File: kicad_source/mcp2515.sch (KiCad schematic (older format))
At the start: 8 parts, among them U8 MCP2515, U9 SN65HVD232, Y1 16MHz

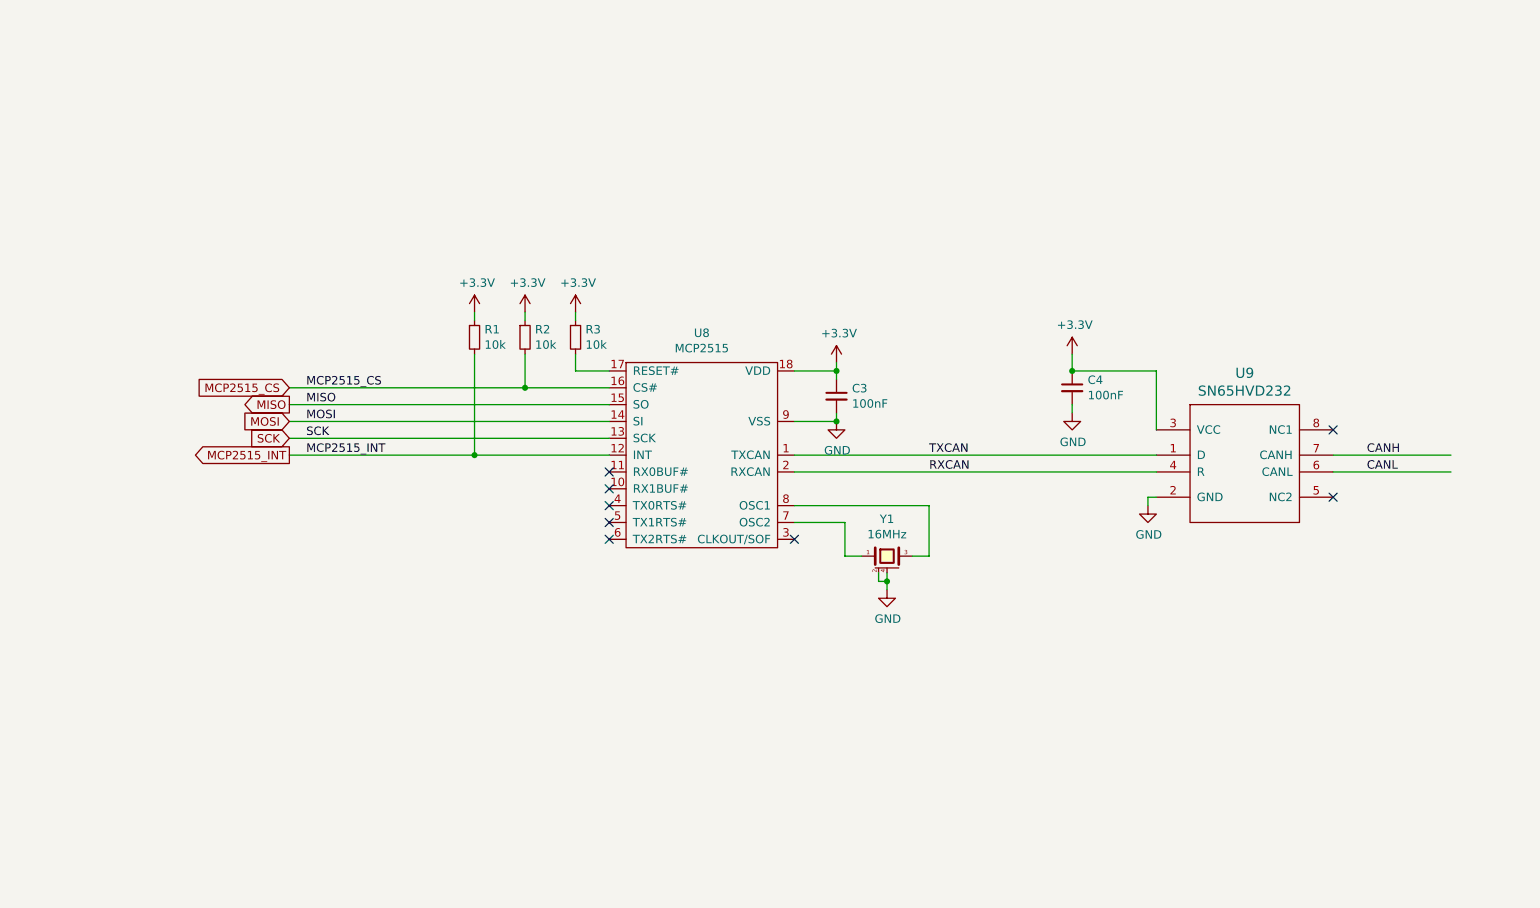
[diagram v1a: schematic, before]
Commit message: added dronecode can and qwiic connectors
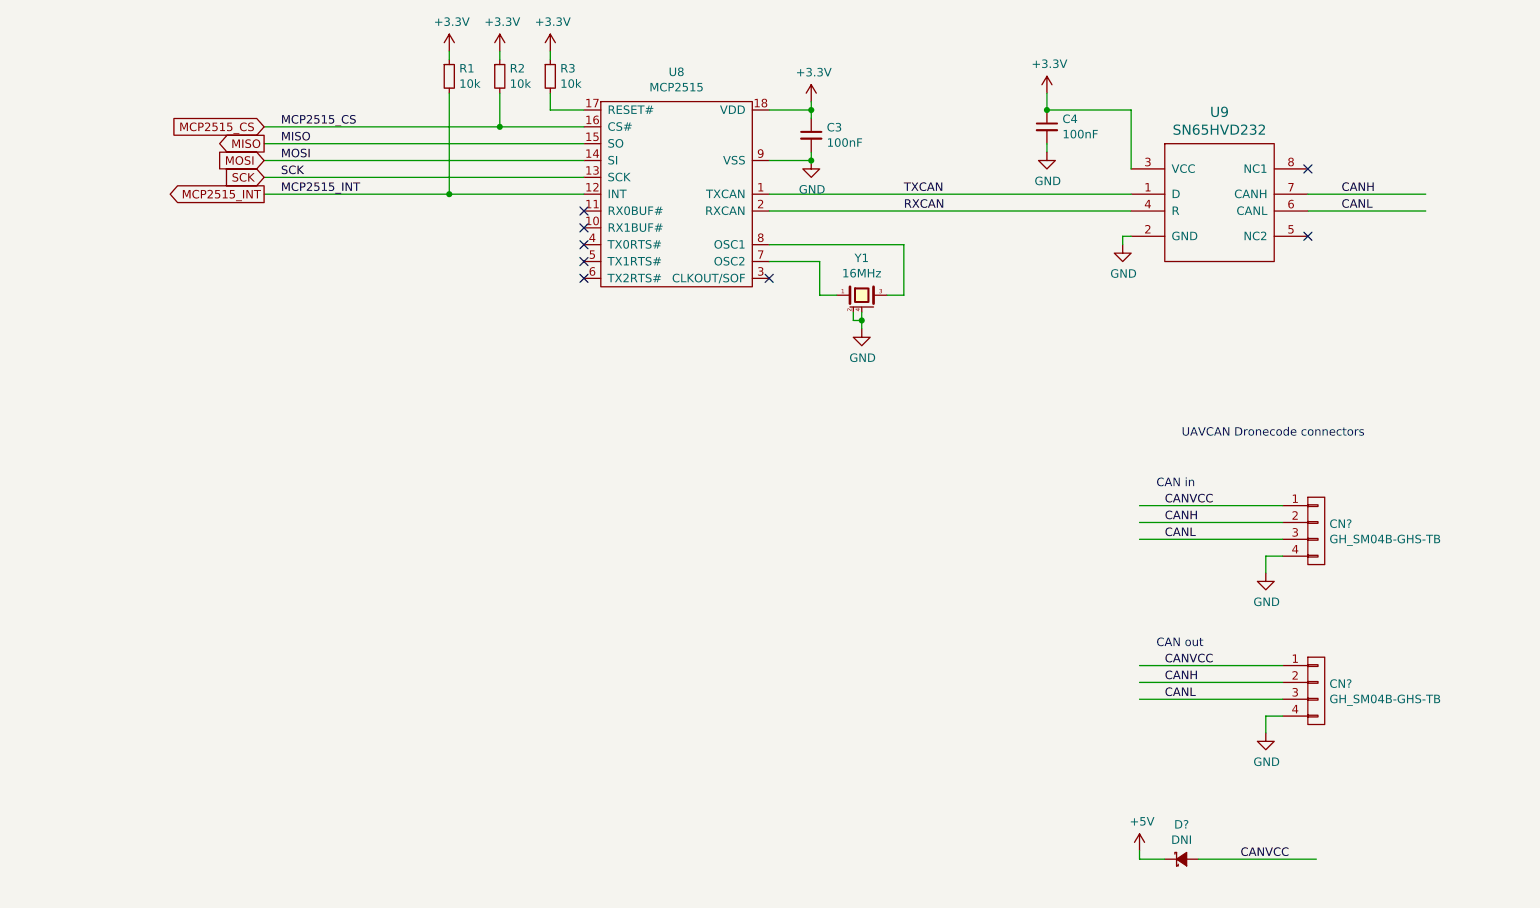
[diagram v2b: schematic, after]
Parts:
- added CN? (x2): GH_SM04B-GHS-TB, Connector_JST:JST_GH_SM04B-GHS-TB_1x04-1MP_P1.25mm_Horizontal, symbol mechanical-connectors:CONN_01X04
- added D?: DNI, diodes:SOD-123, symbol devices:D_Schottky_Small
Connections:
- net labels added: +5V, CANVCC
- wire segments 39 -> 52
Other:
- note added: "CAN in"
- note added: "CAN out"
- note added: "UAVCAN Dronecode connectors"
- moved on the sheet: C3, C4, R1, R2, R3, U8, U9, Y1

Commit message: added eeprom and servo connectors, updated pdf
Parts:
- added C7, C8: 10pF, capacitors:C_0603, symbol devices:C_0603
- gave numbers to parts that had none: 3
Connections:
- wire segments 52 -> 56
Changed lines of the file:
@@
 P 8800 4200
 AR Path="/624F7A5F/62500CA8" Ref="CN?"  Part="1"
-AR Path="/5ED92F9C/62500CA8" Ref="CN?"  Part="1"
-F 0 "CN?" H 8878 4241 50  0000 L CNN
+AR Path="/5ED92F9C/62500CA8" Ref="CN4"  Part="1"
+F 0 "CN4" H 8878 4241 50  0000 L CNN
 F 1 "GH_SM04B-GHS-TB" H 8878 4150 50  0000 L CNN
 F 2 "Connector_JST:JST_GH_SM04B-GHS-TB_1x04-1MP_P1.25mm_Horizontal" H 8800 4200 50  0001 C CNN
@@
 P 8500 4450
 AR Path="/624F7A5F/62500CB2" Ref="#PWR?"  Part="1"
-AR Path="/5ED92F9C/62500CB2" Ref="#PWR?"  Part="1"
-F 0 "#PWR?" H 8500 4200 50  0001 C CNN
+AR Path="/5ED92F9C/62500CB2" Ref="#PWR036"  Part="1"
+F 0 "#PWR036" H 8500 4200 50  0001 C CNN
 F 1 "GND" H 8505 4277 50  0000 C CNN
 F 2 "" H 8500 4450 50  0000 C CNN
@@
 P 8800 5150
 AR Path="/624F7A5F/62500CBC" Ref="CN?"  Part="1"
-AR Path="/5ED92F9C/62500CBC" Ref="CN?"  Part="1"
-F 0 "CN?" H 8878 5191 50  0000 L CNN
+AR Path="/5ED92F9C/62500CBC" Ref="CN5"  Part="1"
+F 0 "CN5" H 8878 5191 50  0000 L CNN
 F 1 "GH_SM04B-GHS-TB" H 8878 5100 50  0000 L CNN
 F 2 "Connector_JST:JST_GH_SM04B-GHS-TB_1x04-1MP_P1.25mm_Horizontal" H 8800 5150 50  0001 C CNN
@@
 P 8500 5400
 AR Path="/624F7A5F/62500CC6" Ref="#PWR?"  Part="1"
-AR Path="/5ED92F9C/62500CC6" Ref="#PWR?"  Part="1"
-F 0 "#PWR?" H 8500 5150 50  0001 C CNN
+AR Path="/5ED92F9C/62500CC6" Ref="#PWR037"  Part="1"
+F 0 "#PWR037" H 8500 5150 50  0001 C CNN
 F 1 "GND" H 8505 5227 50  0000 C CNN
 F 2 "" H 8500 5400 50  0000 C CNN
@@
 P 8000 6150
 AR Path="/624F7A5F/62500CCF" Ref="D?"  Part="1"
-AR Path="/5ED92F9C/62500CCF" Ref="D?"  Part="1"
-F 0 "D?" H 8000 6355 50  0000 C CNN
+AR Path="/5ED92F9C/62500CCF" Ref="D2"  Part="1"
+F 0 "D2" H 8000 6355 50  0000 C CNN
 F 1 "DNI" H 8000 6264 50  0000 C CNN
 F 2 "diodes:SOD-123" V 8000 6150 50  0001 C CNN
@@
 P 7750 6100
 AR Path="/624F7A5F/62500CD5" Ref="#PWR?"  Part="1"
-AR Path="/5ED92F9C/62500CD5" Ref="#PWR?"  Part="1"
-F 0 "#PWR?" H 7750 5950 50  0001 C CNN
+AR Path="/5ED92F9C/62500CD5" Ref="#PWR038"  Part="1"
+F 0 "#PWR038" H 7750 5950 50  0001 C CNN
 F 1 "+5V" H 7765 6273 50  0000 C CNN
 F 2 "" H 7750 6100 50  0000 C CNN
@@
 Wire Wire Line
 	7750 4050 8600 4050
+$Comp
+L devices:C_0603 C8
+U 1 1 62513A43
+P 6350 2950
+F 0 "C8" H 6442 2996 50  0000 L CNN
+F 1 "10pF" H 6442 2905 50  0000 L CNN
+F 2 "capacitors:C_0603" H 6350 2800 50  0001 C CNN
+F 3 "" H 6350 2950 50  0000 C CNN
+	1    6350 2950
+	1    0    0    -1
+$EndComp
+$Comp
+L devices:C_0603 C7
+U 1 1 6251419A
+P 5850 2950
+F 0 "C7" H 5942 2996 50  0000 L CNN
+F 1 "10pF" H 5942 2905 50  0000 L CNN
+F 2 "capacitors:C_0603" H 5850 2800 50  0001 C CNN
+F 3 "" H 5850 2950 50  0000 C CNN
+	1    5850 2950
+	-1   0    0    -1
+$EndComp
+$Comp
+L power-supply:GND #PWR034
+U 1 1 625148D1
+P 5850 3100
+F 0 "#PWR034" H 5850 2850 50  0001 C CNN
+F 1 "GND" H 5855 2927 50  0000 C CNN
+F 2 "" H 5850 3100 50  0000 C CNN
+F 3 "" H 5850 3100 50  0000 C CNN
+	1    5850 3100
+	1    0    0    -1
+$EndComp
+$Comp
+L power-supply:GND #PWR035
+U 1 1 62514AF6
+P 6350 3100
+F 0 "#PWR035" H 6350 2850 50  0001 C CNN
+F 1 "GND" H 6355 2927 50  0000 C CNN
+F 2 "" H 6350 3100 50  0000 C CNN
+F 3 "" H 6350 3100 50  0000 C CNN
+	1    6350 3100
+	1    0    0    -1
+$EndComp
+Wire Wire Line
+	5850 2850 5850 2800
+Connection ~ 5850 2800
+Wire Wire Line
+	6350 2850 6350 2800
+Connection ~ 6350 2800
+Wire Wire Line
+	6350 3050 6350 3100
+Wire Wire Line
+	5850 3050 5850 3100
 $EndSCHEMATC

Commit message: updated connectors, added power input
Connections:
- net labels added: +BATT
- net labels removed: +5V
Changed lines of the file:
@@
-	1    0    0    -1
-$EndComp
-$Comp
-L power-supply:+5V #PWR?
-U 1 1 62500CD5
-P 7750 6100
-AR Path="/624F7A5F/62500CD5" Ref="#PWR?"  Part="1"
-AR Path="/5ED92F9C/62500CD5" Ref="#PWR038"  Part="1"
-F 0 "#PWR038" H 7750 5950 50  0001 C CNN
-F 1 "+5V" H 7765 6273 50  0000 C CNN
-F 2 "" H 7750 6100 50  0000 C CNN
-F 3 "" H 7750 6100 50  0000 C CNN
-	1    7750 6100
 	1    0    0    -1
 $EndComp
@@
 Wire Wire Line
 	5850 3050 5850 3100
+$Comp
+L power-supply:+BATT #PWR038
+U 1 1 6252FED9
+P 7750 6100
+F 0 "#PWR038" H 7750 5950 50  0001 C CNN
+F 1 "+BATT" H 7765 6273 50  0000 C CNN
+F 2 "" H 7750 6100 50  0000 C CNN
+F 3 "" H 7750 6100 50  0000 C CNN
+	1    7750 6100
+	1    0    0    -1
+$EndComp
 $EndSCHEMATC

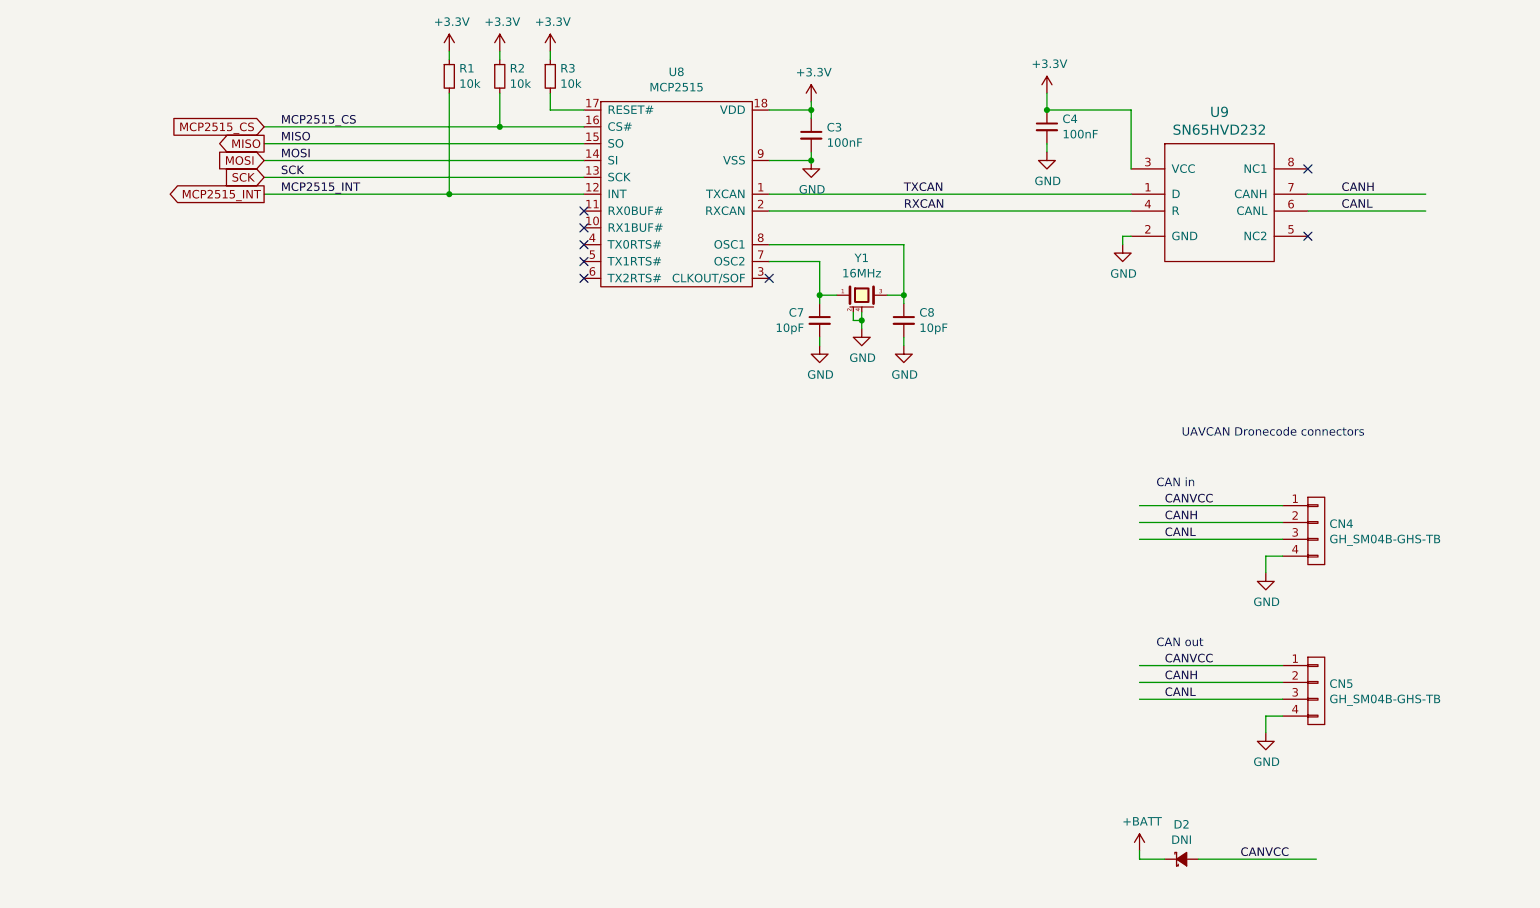
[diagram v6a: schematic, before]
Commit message: added alternative DIL package for MCP2515
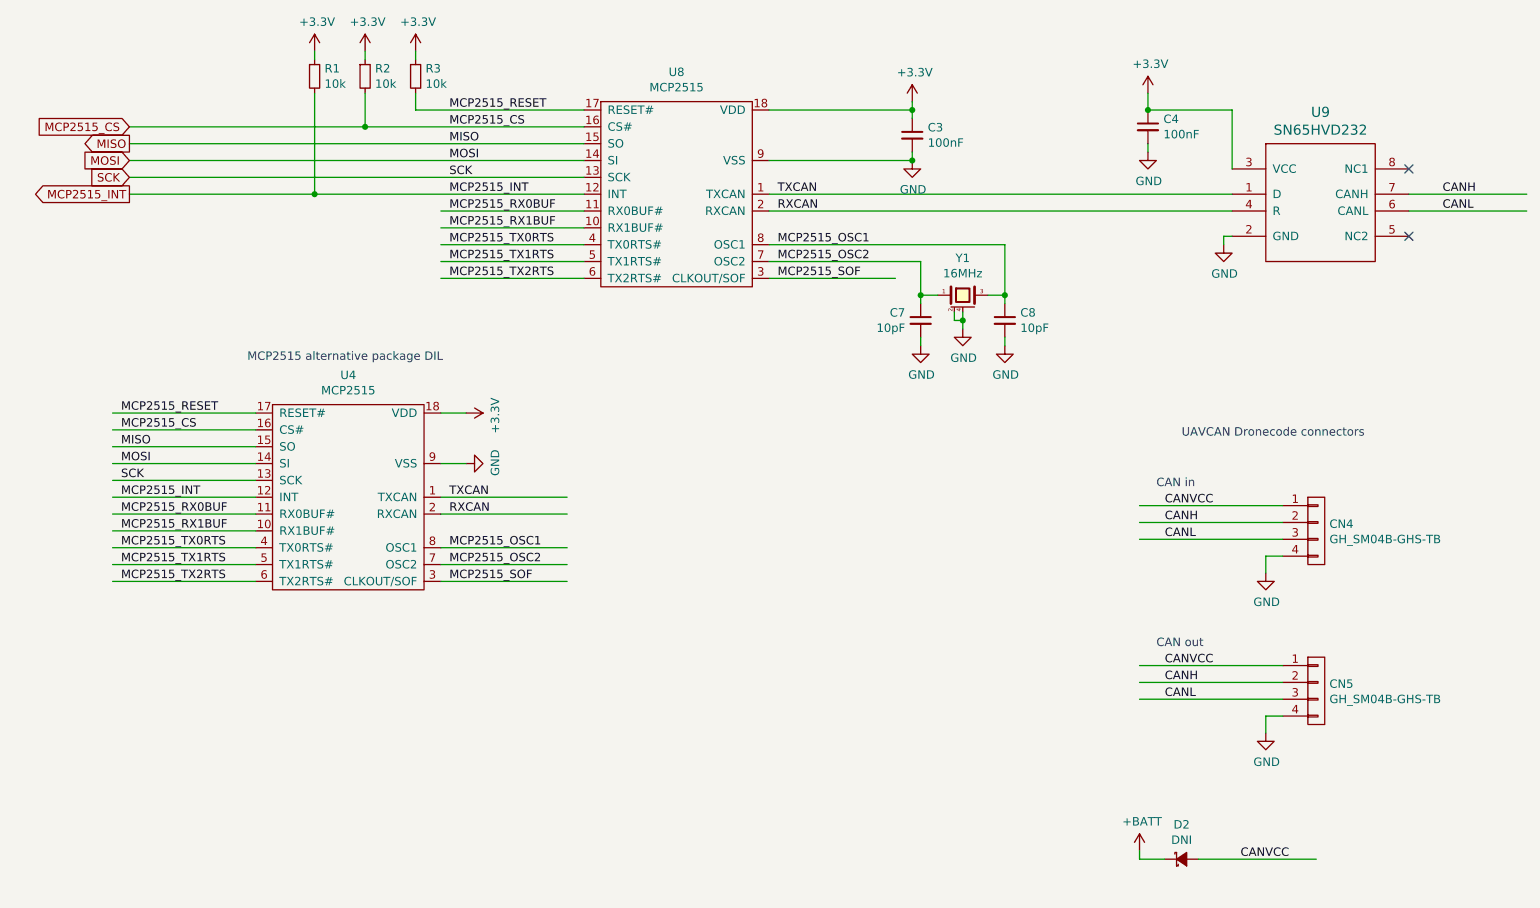
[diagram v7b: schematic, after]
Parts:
- added U4: MCP2515, DIP:DIP-18_W7.62mm, symbol IC_transceiver_can:MCP2515
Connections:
- net labels added: MCP2515_OSC1, MCP2515_OSC2, MCP2515_RESET, MCP2515_RX0BUF, MCP2515_RX1BUF, MCP2515_SOF, MCP2515_TX0RTS, MCP2515_TX1RTS, MCP2515_TX2RTS
- wire segments 56 -> 80
- no-connect marks 8 -> 2
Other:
- note added: "MCP2515 alternative package DIL"
- moved on the sheet: C3, C4, C7, C8, R1, R2, R3, U9, Y1

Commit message: updated BOM in readme and schematic, updated schematic pdf
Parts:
- D2: value DNI -> MBR0530T1G
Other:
- note added: "30V 500mA"
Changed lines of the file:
@@
 AR Path="/5ED92F9C/62500CCF" Ref="D2"  Part="1"
 F 0 "D2" H 8000 6355 50  0000 C CNN
-F 1 "DNI" H 8000 6264 50  0000 C CNN
+F 1 "MBR0530T1G" H 8000 6264 50  0000 C CNN
 F 2 "diodes:SOD-123" V 8000 6150 50  0001 C CNN
 F 3 "" V 8000 6150 50  0000 C CNN
@@
 Text Notes 2450 3200 0    50   ~ 0
 MCP2515 alternative package DIL
+Text Notes 7900 6350 0    50   ~ 0
+30V 500mA
 $EndSCHEMATC
